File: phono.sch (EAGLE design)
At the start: 67 parts, among them IC1 NE5532N, IC2 NE5532N, IC3 NE5532N, J1 12VAC, J2 PHONO, J3 OUT, Q1 BC548B, U2 LM317

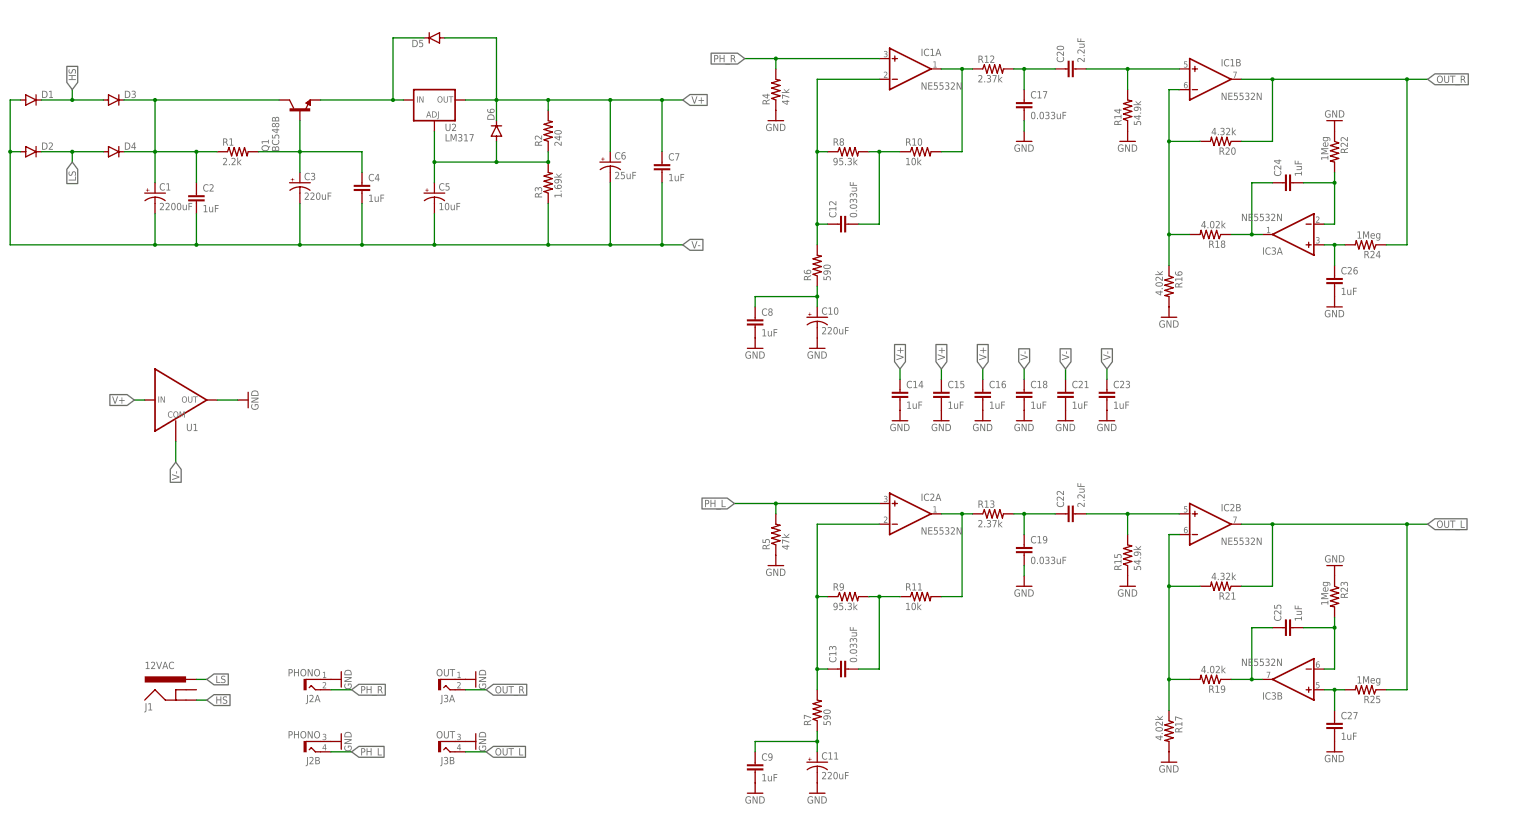
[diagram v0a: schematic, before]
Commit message: 100p input shunt
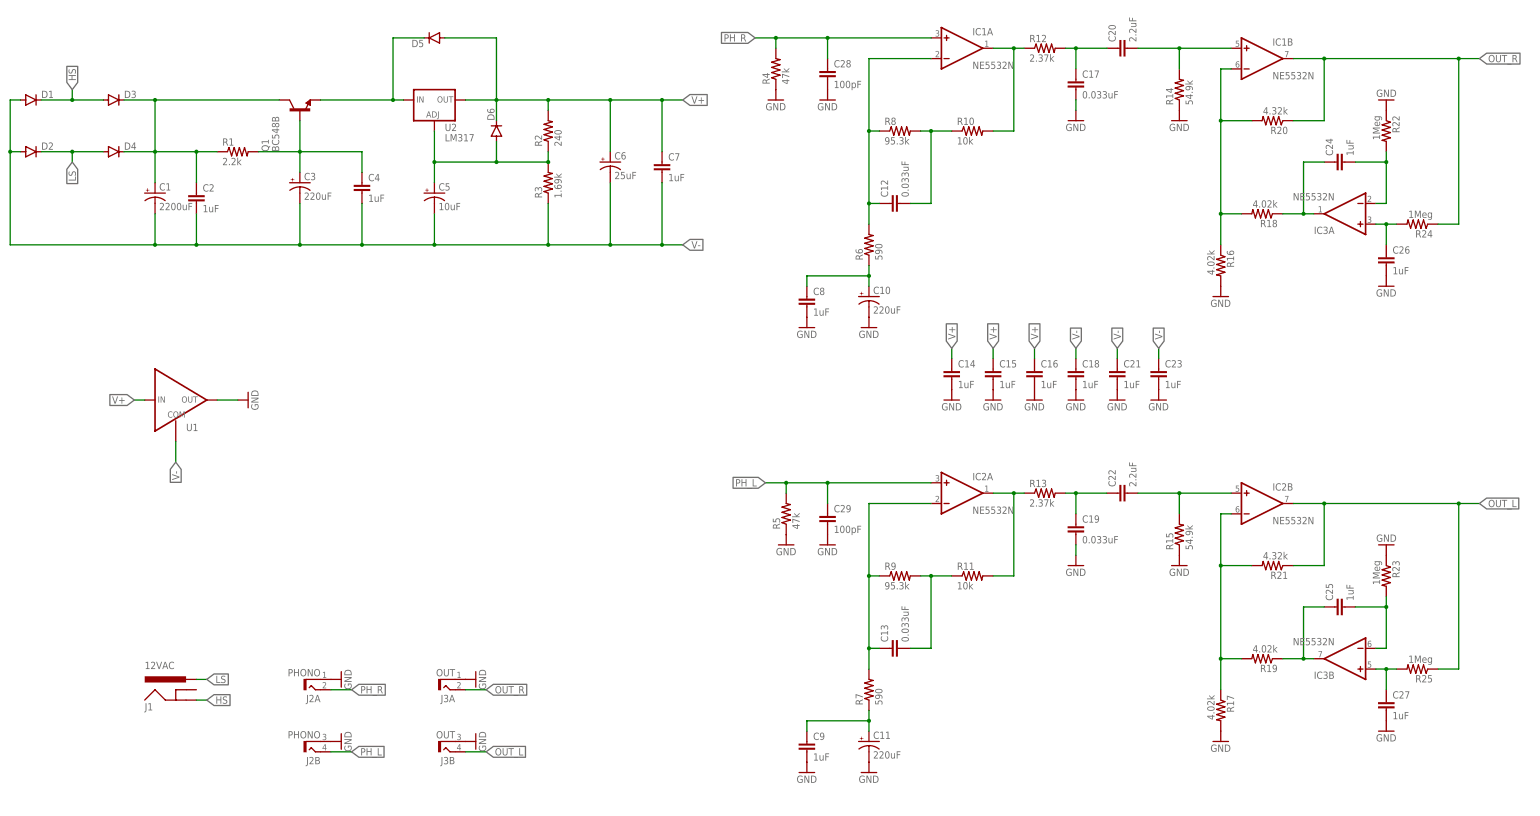
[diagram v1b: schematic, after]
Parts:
- added C28, C29: 100pF, capacitor-wima:C5/4.5
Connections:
- net GND: now also C28.2, C29.2
- net PH_L: now also C29.1
- net PH_R: now also C28.1
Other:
- moved on the sheet: C10, C11, C12, C13, C14, C15, C16, C17, C18, C19, C20, C21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
